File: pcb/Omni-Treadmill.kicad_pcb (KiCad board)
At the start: 2 copper layers, 1 part

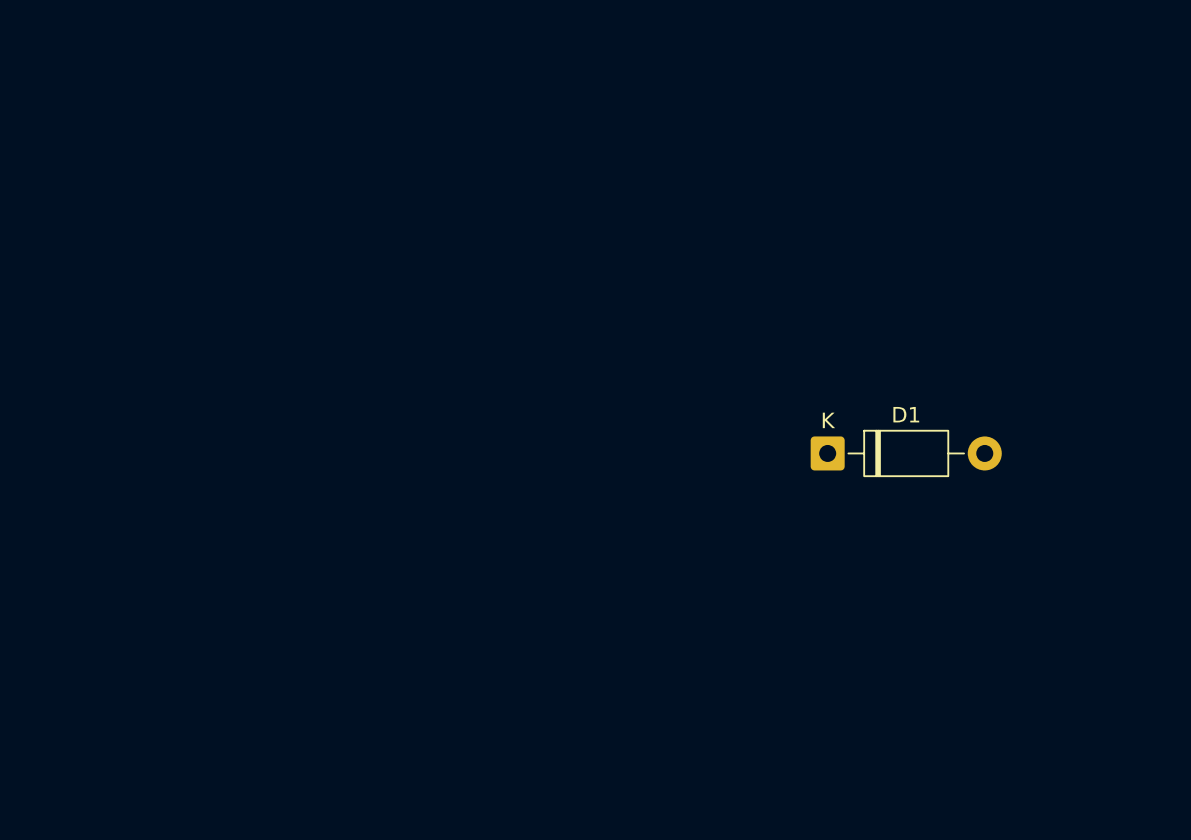
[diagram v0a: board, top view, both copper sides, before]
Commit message: updated hbridge and components
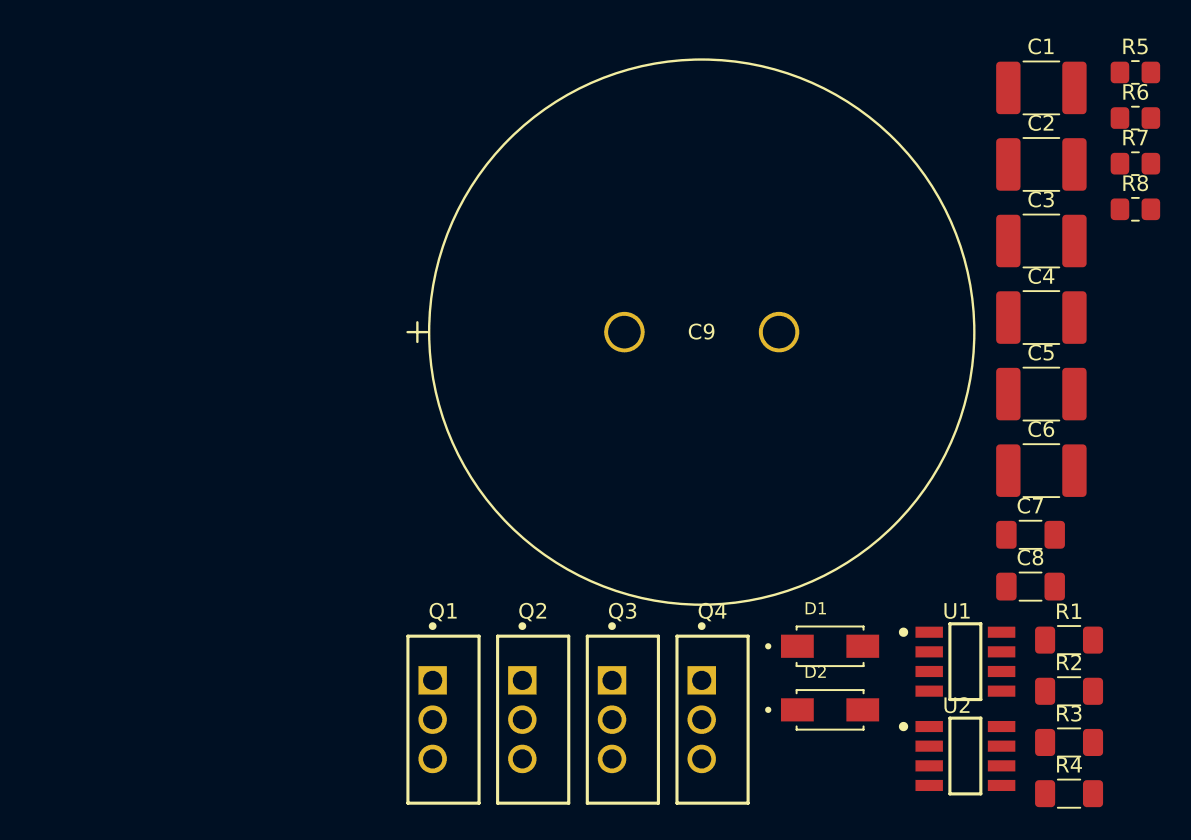
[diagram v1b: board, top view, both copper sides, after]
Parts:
- added C1: 1 uF, Capacitor_SMD:C_1812_4532Metric_Pad1.57x3.40mm_HandSolder, F.Cu at (165.7, 64.9)
- added C2: 470 nF, Capacitor_SMD:C_1812_4532Metric_Pad1.57x3.40mm_HandSolder, F.Cu at (165.7, 69.8)
- added C3: 1 uF, Capacitor_SMD:C_1812_4532Metric_Pad1.57x3.40mm_HandSolder, F.Cu at (165.7, 74.8)
- added C4: 1 uF, Capacitor_SMD:C_1812_4532Metric_Pad1.57x3.40mm_HandSolder, F.Cu at (165.7, 79.7)
- added C5: 470 nF, Capacitor_SMD:C_1812_4532Metric_Pad1.57x3.40mm_HandSolder, F.Cu at (165.7, 84.7)
- added C6: 1 uF, Capacitor_SMD:C_1812_4532Metric_Pad1.57x3.40mm_HandSolder, F.Cu at (165.7, 89.6)
- added C7: 100 nF, Capacitor_SMD:C_1206_3216Metric_Pad1.33x1.80mm_HandSolder, F.Cu at (165.0, 93.8)
- added C8: 100 nF, Capacitor_SMD:C_1206_3216Metric_Pad1.33x1.80mm_HandSolder, F.Cu at (165.0, 97.1)
- added C9: LGW2D821MELC25, Library:CAP_C25_NCH, F.Cu at (138.7, 80.7)
- added D2: ES1J, Library:DIOM4325X250N, F.Cu at (152.0, 105.1)
- added Q1: IRFB4020, Library:IFX-PG-TO220-3-904, F.Cu at (126.3, 105.7)
- added Q2: IRFB4020, Library:IFX-PG-TO220-3-904, F.Cu at (132.1, 105.7)
- added Q3: IRFB4020, Library:IFX-PG-TO220-3-904, F.Cu at (137.9, 105.7)
- added Q4: IRFB4020, Library:IFX-PG-TO220-3-904, F.Cu at (143.7, 105.7)
- added R1: 10, Resistor_SMD:R_1206_3216Metric_Pad1.30x1.75mm_HandSolder, F.Cu at (167.4, 100.6)
- added R2: 10, Resistor_SMD:R_1206_3216Metric_Pad1.30x1.75mm_HandSolder, F.Cu at (167.4, 103.9)
- added R3: 10, Resistor_SMD:R_1206_3216Metric_Pad1.30x1.75mm_HandSolder, F.Cu at (167.4, 107.2)
- added R4: 10, Resistor_SMD:R_1206_3216Metric_Pad1.30x1.75mm_HandSolder, F.Cu at (167.4, 110.5)
- added R5: 10k, Resistor_SMD:R_0805_2012Metric_Pad1.20x1.40mm_HandSolder, F.Cu at (171.7, 63.9)
- added R6: 10k, Resistor_SMD:R_0805_2012Metric_Pad1.20x1.40mm_HandSolder, F.Cu at (171.7, 66.8)
- added R7: 10k, Resistor_SMD:R_0805_2012Metric_Pad1.20x1.40mm_HandSolder, F.Cu at (171.7, 69.8)
- added R8: 10k, Resistor_SMD:R_0805_2012Metric_Pad1.20x1.40mm_HandSolder, F.Cu at (171.7, 72.7)
- added U1: IRS2184S, Library:SOIC127P600X175-8N-12-V, F.Cu at (160.7, 102.0)
- added U2: IRS2184S, Library:SOIC127P600X175-8N-12-V, F.Cu at (160.7, 108.1)
- D1: value 1N4001 -> ES1J; footprint Diode_THT:D_DO-41_SOD81_P10.16mm_Horizontal -> Library:DIOM4325X250N
- moved D1 12.5 mm to (152.0, 101.0)

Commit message: layout complete - needs trace routing
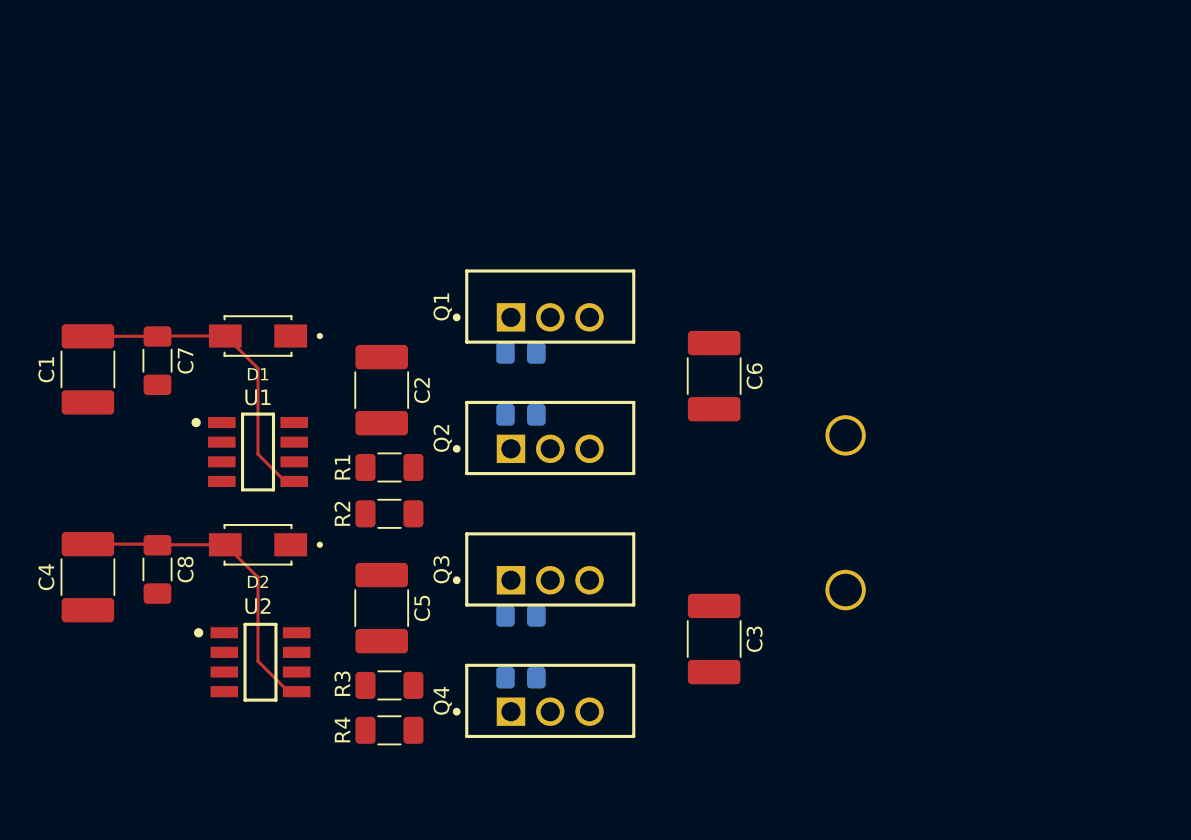
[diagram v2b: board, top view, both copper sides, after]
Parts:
- C9, R5, R6, R7, R8: moved to B.Cu
- moved C1 64.3 mm to (104.0, 83.1), turned to 90 degrees
- moved C4 63.9 mm to (104.0, 96.5), turned to 90 degrees
- moved C7 57.6 mm to (108.5, 82.5), turned to -90 degrees
- moved C8 56.5 mm to (108.5, 96.0), turned to -90 degrees
- moved R6 51.1 mm to (132.0, 99.0), turned to 180 degrees
- moved R8 50.0 mm to (132.0, 103.0), turned to 180 degrees
- moved U1 47.7 mm to (115.0, 88.4)
- moved U2 46.0 mm to (115.2, 102.0)
- moved R2 45.4 mm to (123.5, 92.4)
- moved R1 45.3 mm to (123.5, 89.4)
- moved C2 45.1 mm to (123.0, 84.4), turned to -90 degrees
- moved C5 44.8 mm to (123.0, 98.5), turned to -90 degrees
- moved R4 44.1 mm to (123.5, 106.4)
- moved R3 44.1 mm to (123.5, 103.5)
- moved R5 43.7 mm to (132.0, 82.0), turned to 180 degrees
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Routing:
- net VCC: track 0.00 -> 41.8 mm
- added copper zone on In1.Cu, net GND
- added copper zone on In2.Cu, net GND
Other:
- copper layers 2 -> 4
